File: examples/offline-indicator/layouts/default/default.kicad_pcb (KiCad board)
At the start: 2 copper layers, 32 x 18 mm, 3 parts

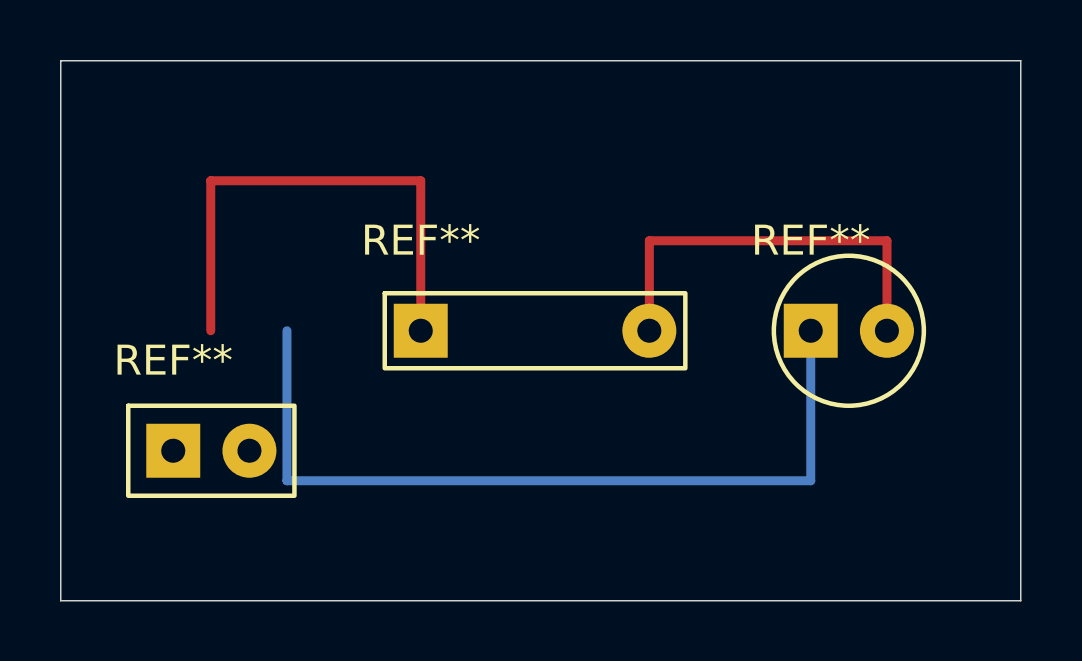
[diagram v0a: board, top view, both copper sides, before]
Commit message: Keep the release demo at its verified placement
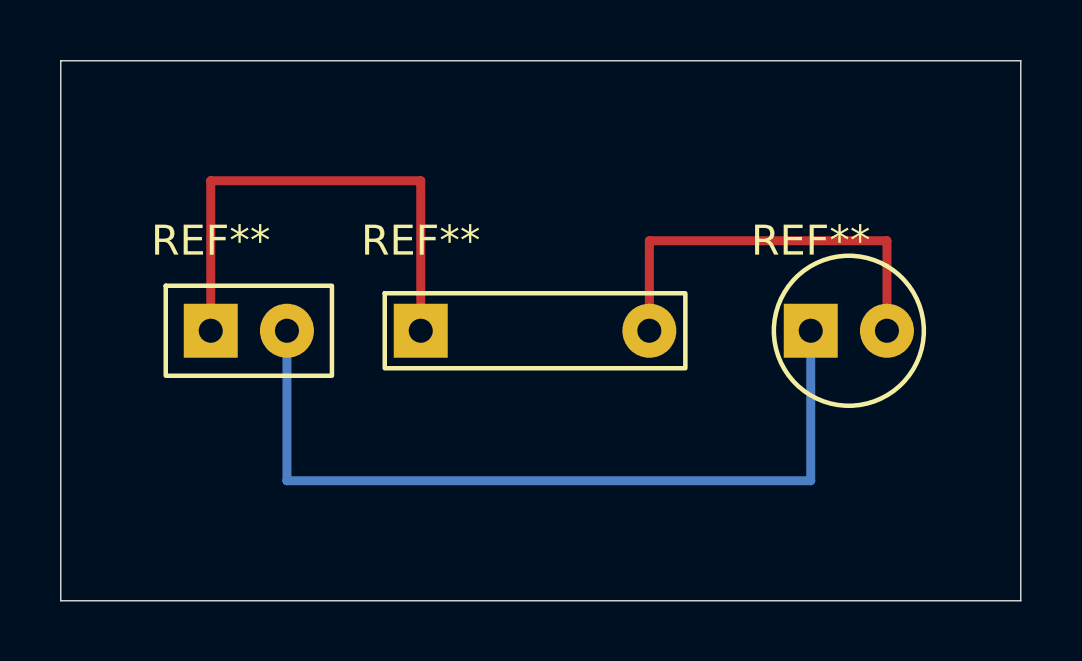
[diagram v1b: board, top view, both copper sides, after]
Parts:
- moved J1 4.19 mm to (5.00, 9.00)
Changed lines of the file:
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@@
 	(footprint "Local_Input2:Input2"
 		(layer "F.Cu")
-		(at 3.75 13 0)
+		(at 5 9 0)
 		(property "LCSC" "MANUAL-Input2"
 			(at 0 0 0)

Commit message: Restore Codex board tools and bind chat to the selected PCB
Keep the dynamic tool host enabled, inspect the actual board before local inference, and show the agent identity and last board read. Preserve selected targets and saved conversation IDs, restore chats at startup, and keep placement backups and cancellation from breaking subsequent board operations. Release Atopile Local 0.3.1 with full-catalog and installed-chat verification.
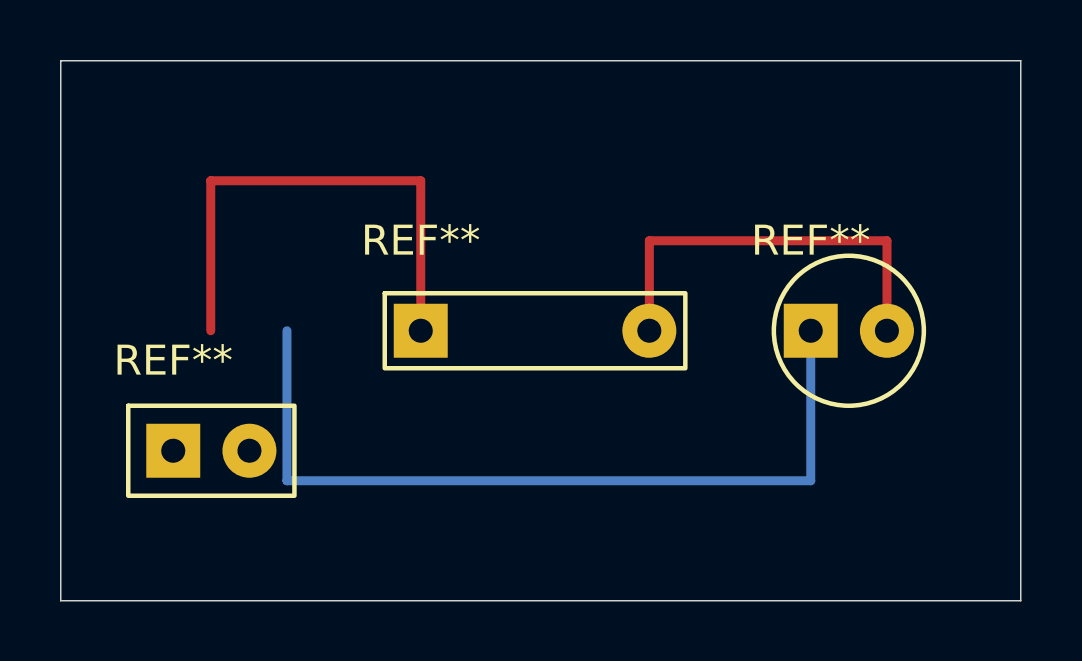
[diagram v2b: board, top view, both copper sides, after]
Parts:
- moved J1 4.19 mm to (3.75, 13.0)
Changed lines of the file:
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@@
 	(footprint "Local_Input2:Input2"
 		(layer "F.Cu")
-		(at 5 9 0)
+		(at 3.75 13 0)
 		(property "LCSC" "MANUAL-Input2"
 			(at 0 0 0)
